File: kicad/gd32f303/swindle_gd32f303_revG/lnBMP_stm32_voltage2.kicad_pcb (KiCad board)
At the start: 2 copper layers, 49.2 x 31.7 mm, 56 parts, among them J1 Debug port, J2 Debug port, J3 USB, J4 DFU, J5 BOOT, J6 jtag, J9 Conn_01x03_Socket, U1 GD32F303, U2 3V->VTREF, U3 VTREF->3V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

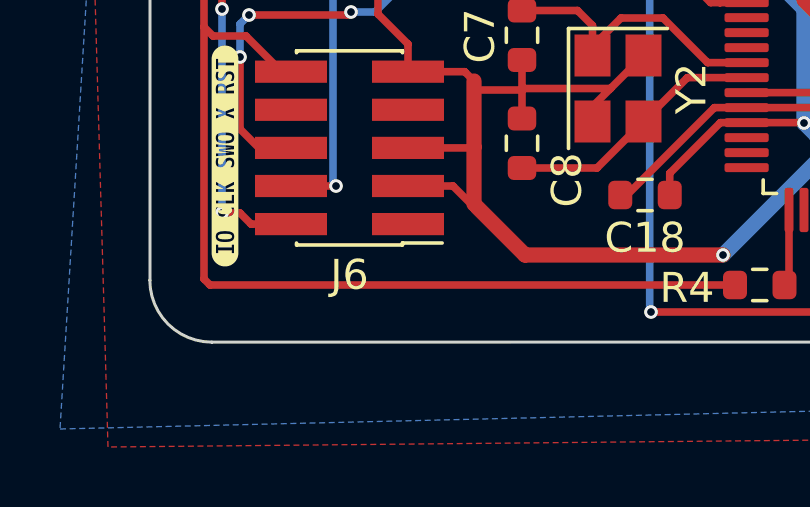
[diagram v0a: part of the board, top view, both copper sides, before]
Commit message: kicad: rename to GD32F303
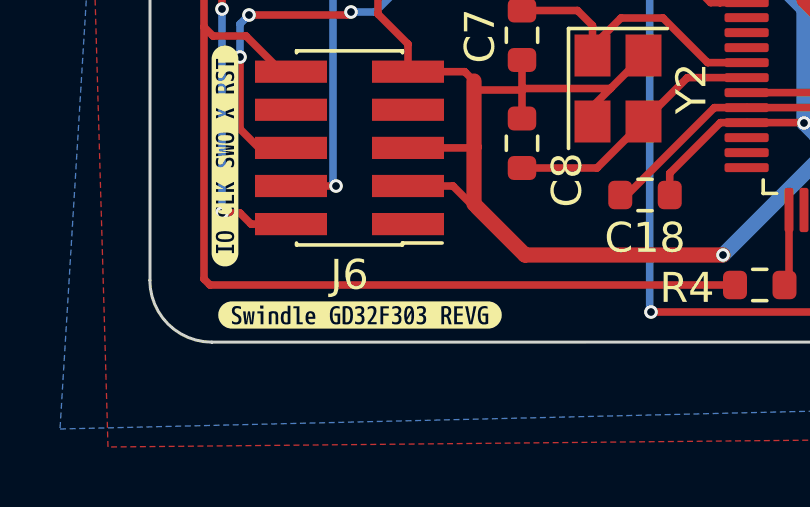
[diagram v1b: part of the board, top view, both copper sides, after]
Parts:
- added kibuzzard-672326BE: G***, kibuzzard-672326BE, F.Cu at (113.2, 99.1)
